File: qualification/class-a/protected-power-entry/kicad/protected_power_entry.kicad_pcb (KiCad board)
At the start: 2 copper layers, 81 x 32 mm, 84 parts, among them J1 (no value), J2 M20-9990846, J3 (no value), J4 (no value), J5 (no value), Q1 (no value), U1 MP2307DN-LF-Z, U2 AMS1117-3.3, U3 TPS22918DBVR

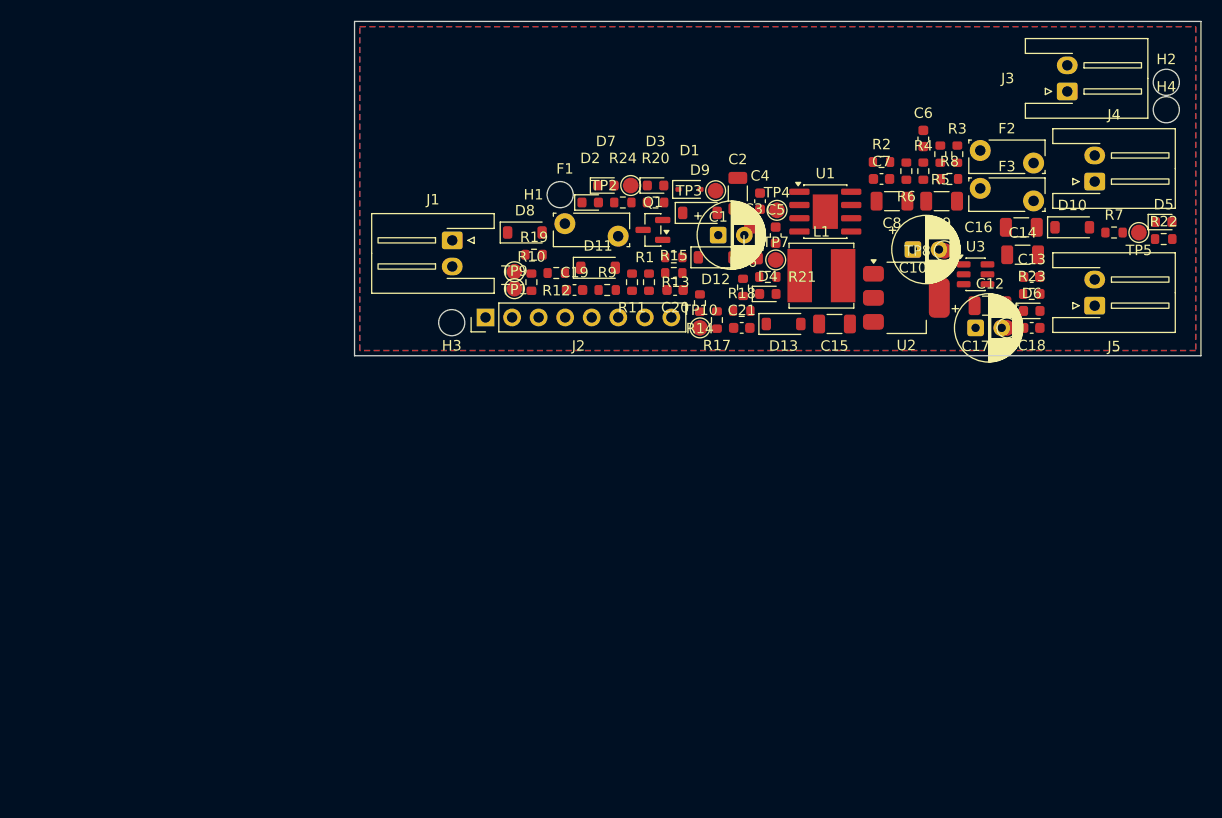
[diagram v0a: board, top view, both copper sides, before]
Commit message: feat: route protected-power-entry with kicad-routing-tools (0 unconnected pads)
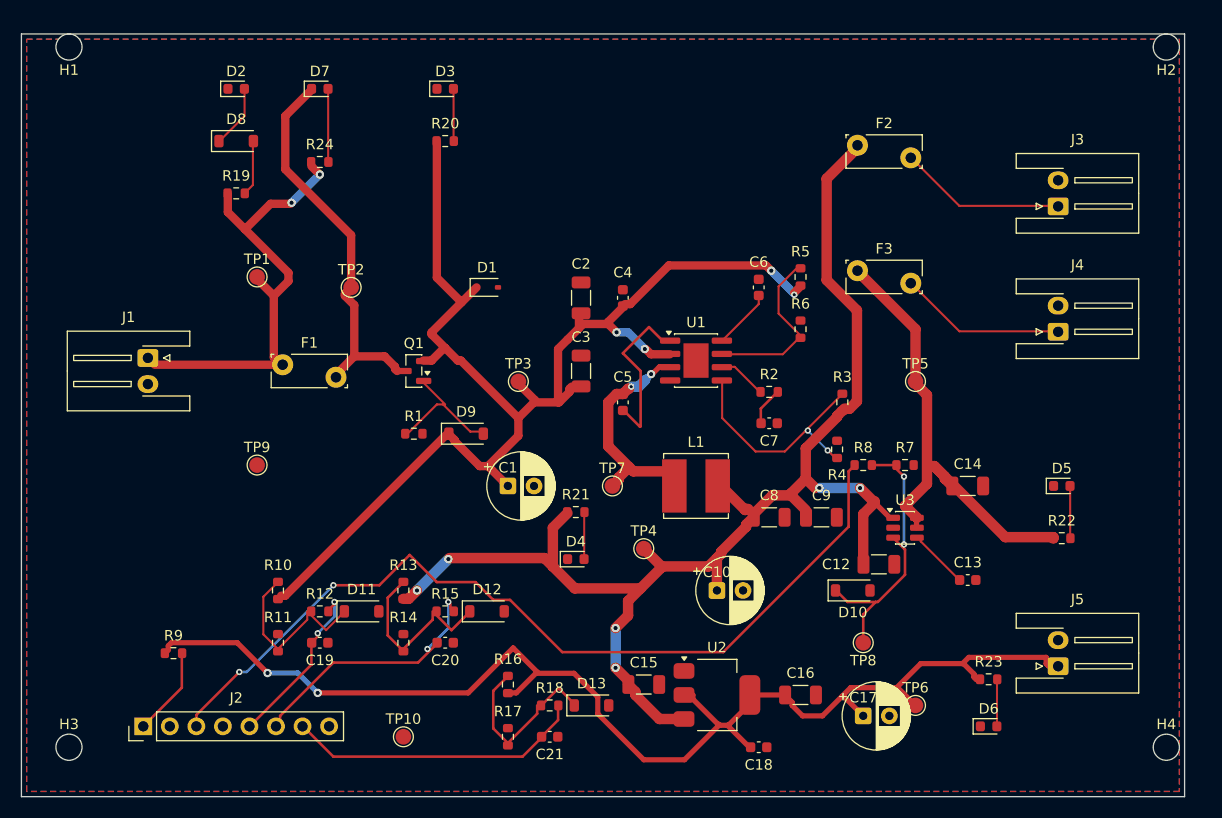
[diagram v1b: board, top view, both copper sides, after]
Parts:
- moved H4 61.0 mm to (109.0, 71.0)
- moved H3 54.7 mm to (4.00, 71.0)
- moved R9 54.1 mm to (14.0, 62.0)
- moved J2 51.0 mm to (11.1, 69.0)
- moved C16 49.5 mm to (74.0, 66.0)
- moved H1 49.1 mm to (4.00, 4.00)
- moved R11 48.4 mm to (24.0, 61.0)
- moved TP10 48.3 mm to (36.0, 70.0)
- moved C18 47.9 mm to (70.0, 71.0)
- moved R17 44.6 mm to (46.0, 70.0)
- moved R16 44.2 mm to (46.0, 65.0)
- moved C21 43.2 mm to (50.0, 70.0)
- moved R14 43.1 mm to (36.0, 61.0)
- moved U2 42.1 mm to (66.0, 66.0)
- moved R18 42.0 mm to (50.0, 67.0)
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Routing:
- net +5V: track 0.00 -> 131.4 mm, vias 0 -> 6
- net +12V_PROT: track 0.00 -> 122.8 mm, vias 0 -> 4
- net +3V3: track 0.00 -> 121.8 mm, vias 0 -> 2
- net EN_HDR: track 0.00 -> 84.5 mm, vias 0 -> 2
- net +5V_SW: track 0.00 -> 46.4 mm
- net VIN_12V_RAW: track 0.00 -> 44.4 mm, vias 0 -> 2
- net VIN_12V_FUSED: track 0.00 -> 37.0 mm
- net SENSE_3V3: track 0.00 -> 28.4 mm
- net LOAD_EN: track 0.00 -> 26.4 mm, vias 0 -> 2
- net SENSE_5V: track 0.00 -> 24.2 mm, vias 0 -> 2
- net BUCK_FB: track 0.00 -> 22.2 mm, vias 0 -> 2
- net BUCK_SW: track 0.00 -> 20.5 mm, vias 0 -> 2
- net S5_DIV: track 0.00 -> 17.3 mm
- net S12_DIV: track 0.00 -> 16.7 mm
- net S3_DIV: track 0.00 -> 16.7 mm
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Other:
- board size 81 x 32 mm -> 111.3 x 73 mm
- net class Default removed
- net class PGND removed
- net class PWR12 removed
- net class PWR3 removed
- net class PWR5 removed
- net class SIG removed

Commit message: docs: add 3D model screenshots (top, bottom, angled) (SYN-269)
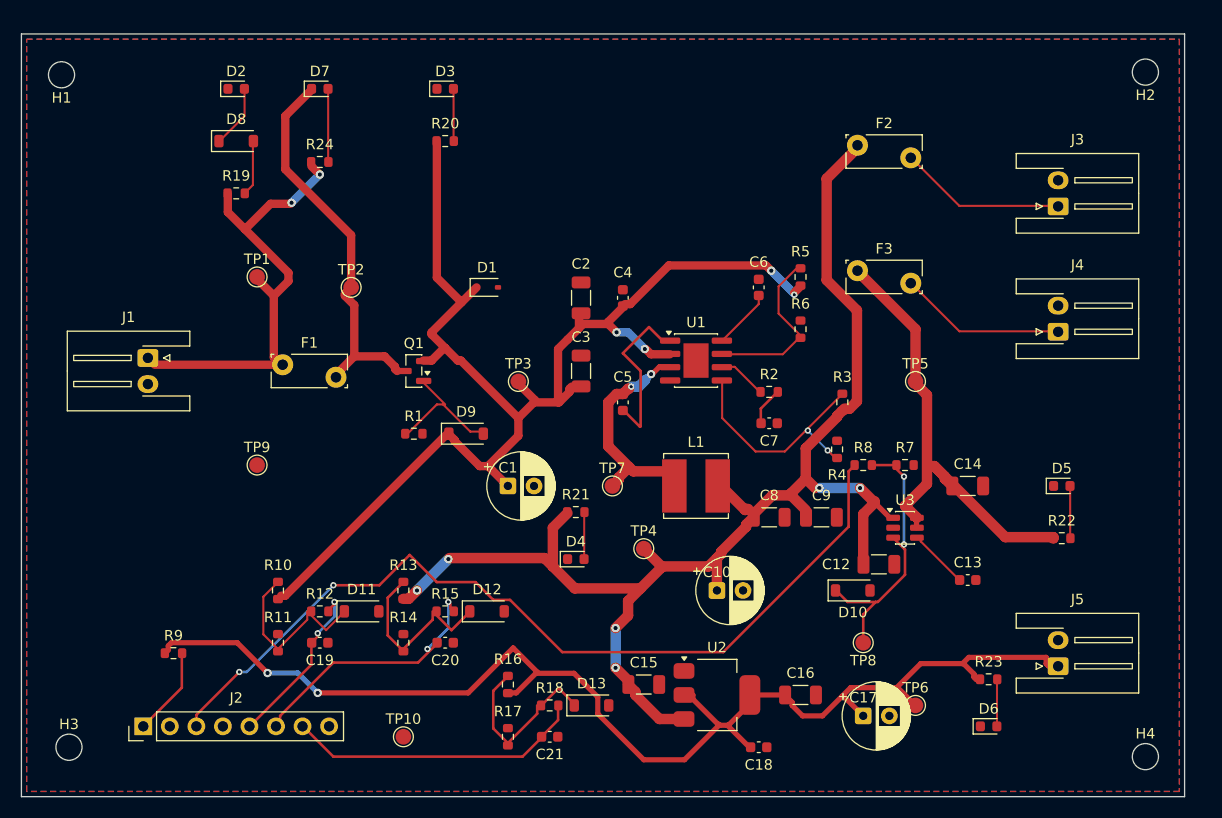
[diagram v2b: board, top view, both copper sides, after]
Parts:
- moved H2 3.12 mm to (107.0, 6.40)
- moved H1 2.75 mm to (3.29, 6.66)
- moved H4 2.19 mm to (107.0, 71.9)
